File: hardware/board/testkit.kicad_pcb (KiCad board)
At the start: 2 copper layers, 100 x 100 mm, 133 parts, among them J1 Power, J12 OSC A, J13 OSC B, J14 OSC C, J15 OSC D, J3 USB_B, J4 Tag-Connect_SWD_TC2030, J5 Left, J6 Right, J7 Bottom, J8 AUDIO IN, J9 AUDIO OUT, SW1 POWER, SW2 Reset, U1 INA219BxDCN, U10 OPA4197, U11 MCP6004, U12 MCP6004, U13 MCP6004, U2 INA219BxDCN, U3 TLV76733, U4 LM4040-10, U5 ATSAMD51J20A-M, U6 AD5685R?RUZ, U7 ADG1414BRU, U8 ADG1414BRU, U9 ADG1414BRU, Y1 32.768 kHz

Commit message: Re-do the motherboard
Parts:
- removed the C20 at (94.0, 116.0)
- removed J12: OSC A, Connector_Audio:Jack_3.5mm_CUI_SJ1-3533NG_Horizontal
- removed J13: OSC B, Connector_Audio:Jack_3.5mm_CUI_SJ1-3533NG_Horizontal
- removed J14: OSC C, Connector_Audio:Jack_3.5mm_CUI_SJ1-3533NG_Horizontal
- removed J15: OSC D, Connector_Audio:Jack_3.5mm_CUI_SJ1-3533NG_Horizontal
- removed R38, R40, R42, R48, R50, R52, R54: 121k, Resistor_SMD:R_0603_1608Metric_Pad0.98x0.95mm_HandSolder
- removed R39, R41, R47, R49, R51, R53: 100k, Resistor_SMD:R_0603_1608Metric_Pad0.98x0.95mm_HandSolder
- removed R43, R44, R45, R46, R55, R56, R57, R58: 18.7k, Resistor_SMD:R_0603_1608Metric_Pad0.98x0.95mm_HandSolder
- removed R59, R60: 1k, Resistor_SMD:R_0603_1608Metric_Pad0.98x0.95mm_HandSolder
- removed REF** (x4): MountingHole_3.2mm_M3, MountingHole:MountingHole_3.2mm_M3
- removed U12, U13: MCP6004, Package_SO:TSSOP-14_4.4x5mm_P0.65mm
- added ?: , winterbloom:ermine, F.Cu at (151.4, 78.7)
- added C18: 1uF, Capacitor_SMD:C_0603_1608Metric_Pad1.08x0.95mm_HandSolder, F.Cu at (134.7, 120.9)
- added D4: 3.3, winterbloom:LED_0805_Kingbright_APT2012, F.Cu at (107.0, 54.0)
- added D5: +12V, winterbloom:LED_0805_Kingbright_APT2012, F.Cu at (104.0, 54.0)
- added D6: -12V, winterbloom:LED_0805_Kingbright_APT2012, F.Cu at (101.0, 54.0)
- added D7: ACT, winterbloom:LED_0805_Kingbright_APT2012, F.Cu at (113.0, 54.0)
- added D8: VBUS, winterbloom:LED_0805_Kingbright_APT2012, F.Cu at (110.0, 54.0)
- added G***: LOGO, winterbloom:Extra_Long_Wiggly_Boi_40mm, F.Cu at (109.8, 131.5)
- added H1: M3, MountingHole:MountingHole_3.2mm_M3_Pad_Via, F.Cu at (80.0, 54.0)
- added H2: M3, MountingHole:MountingHole_3.2mm_M3_Pad_Via, F.Cu at (80.0, 144.0)
- added H3: M3, MountingHole:MountingHole_3.2mm_M3_Pad_Via, F.Cu at (170.0, 54.0)
- added H4: M3, MountingHole:MountingHole_3.2mm_M3_Pad_Via, F.Cu at (170.0, 144.0)
- added J2: SWD, Connector_PinHeader_1.27mm:PinHeader_2x05_P1.27mm_Vertical, F.Cu at (124.2, 69.9)
- C1: value 4.7uF -> 47uF; footprint Capacitor_SMD:C_0805_2012Metric_Pad1.18x1.45mm_HandSolder -> Capacitor_THT:CP_Radial_D5.0mm_P2.50mm
- C17: value 1uF -> 0.1uF
- C2: value 0.1uF -> 47uF; footprint Capacitor_SMD:C_0603_1608Metric_Pad1.08x0.95mm_HandSolder -> Capacitor_THT:CP_Radial_D5.0mm_P2.50mm
- C25, C26, C27, C28, C29, C30, C31, C32: value 22pF -> 0.1uF
- C3: value 0.1uF -> 10uF; footprint Capacitor_SMD:C_0603_1608Metric_Pad1.08x0.95mm_HandSolder -> Capacitor_THT:CP_Radial_D5.0mm_P2.50mm
- C4: value 4.7uF -> 10uF; footprint Capacitor_SMD:C_0805_2012Metric_Pad1.18x1.45mm_HandSolder -> Capacitor_THT:CP_Radial_D5.0mm_P2.50mm
- C5: value 0.1uF -> 4.7nF
- D1, D2: value 1N5819 -> BARRIER; footprint Diode_SMD:D_SOD-123 -> winterbloom:DIODE_SOD-123_SOD-123F
- J1: value Power -> POWER; footprint Connector_PinHeader_2.54mm:PinHeader_2x05_P2.54mm_Horizontal -> Connector_Wire:SolderWire-0.75sqmm_1x03_P4.8mm_D1.25mm_OD2.3mm
- J3: value USB_B -> USB_B_Receptacle
- J4: value Tag-Connect_SWD_TC2030 -> EXT; footprint winterbloom:Tag_Connect_TC2030NL -> Connector_Wire:SolderWire-0.75sqmm_1x06_P4.8mm_D1.25mm_OD2.3mm
- J8: value AUDIO IN -> EXT; footprint Connector_Audio:Jack_3.5mm_CUI_SJ1-3533NG_Horizontal -> Connector_Wire:SolderWire-0.75sqmm_1x06_P4.8mm_D1.25mm_OD2.3mm
- J9: value AUDIO OUT -> EXT; footprint Connector_Audio:Jack_3.5mm_CUI_SJ1-3533NG_Horizontal -> Connector_Wire:SolderWire-0.75sqmm_1x06_P4.8mm_D1.25mm_OD2.3mm
- R1, R2: value 1R -> 1k; footprint Resistor_SMD:R_1210_3225Metric_Pad1.30x2.65mm_HandSolder -> Resistor_SMD:R_0603_1608Metric_Pad0.98x0.95mm_HandSolder
- R3: value 270 -> 1k
- R35, R37: value 100k -> 1k
- R36: value 121k -> 1k
- R5: value 1k -> 1M; footprint Resistor_SMD:R_0603_1608Metric_Pad0.98x0.95mm_HandSolder -> Resistor_SMD:R_0805_2012Metric_Pad1.20x1.40mm_HandSolder
- SW1: footprint Connector_PinSocket_2.54mm:PinSocket_2x02_P2.54mm_Vertical -> Connector_Wire:SolderWire-0.75sqmm_1x04_P4.8mm_D1.25mm_OD2.3mm
- U1: value INA219BxDCN -> LD1117-3.3; footprint Package_TO_SOT_SMD:SOT-23-8 -> Package_TO_SOT_SMD:SOT-223-3_TabPin2
- U2: value INA219BxDCN -> LM4040-10; footprint Package_TO_SOT_SMD:SOT-23-8 -> Package_TO_SOT_SMD:SOT-23
- U3: value TLV76733 -> LM4040-10; footprint winterbloom:TI-DGN-HVSSOP-8_3.0x3.0mm_P0.65mm -> Package_TO_SOT_SMD:SOT-23
- U4: value LM4040-10 -> MUX509; footprint Package_TO_SOT_SMD:SOT-23 -> Package_SO:TSSOP-16_4.4x5mm_P0.65mm
- U7, U8, U9: value ADG1414BRU -> MUX509; footprint Package_SO:TSSOP-24_4.4x7.8mm_P0.65mm -> Package_SO:TSSOP-16_4.4x5mm_P0.65mm
- moved R5 75.1 mm to (116.0, 54.0), turned to 90 degrees
- moved U7 73.2 mm to (89.7, 112.1), turned to 0 degrees
- moved U8 70.5 mm to (89.6, 121.1), turned to 0 degrees
- moved C30 67.2 mm to (159.3, 129.4), turned to 0 degrees
- moved U4 66.1 mm to (157.1, 133.6), turned to 0 degrees
- moved R36 64.9 mm to (151.1, 119.5)
- moved U2 64.7 mm to (148.1, 119.5), turned to 180 degrees
- moved R6 63.6 mm to (113.2, 59.0), turned to 90 degrees
- moved C32 52.0 mm to (159.7, 120.7), turned to 0 degrees
- moved C27 51.9 mm to (154.9, 129.4), turned to 180 degrees
- moved C28 50.1 mm to (154.9, 120.7), turned to 180 degrees
- moved R35 47.5 mm to (111.0, 59.0)
- moved U3 43.1 mm to (97.7, 111.5), turned to 270 degrees
- moved J3 39.4 mm to (124.7, 62.2), turned to 90 degrees
- moved C1 35.1 mm to (93.0, 62.0)
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- renumbered C18 to C20
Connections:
- net D+ renamed /MCU/D+
- net D- renamed /MCU/D-
- net DAC_1 renamed /DAC/DAC_1
- net DAC_3 renamed /DAC/DAC_3
- net Net-(U6-Pad1) renamed /DAC/DAC_VREF
- C1 pad 1: +12V -> +12VRAW
- C15 pad 1: +3V3 -> GND
- C15 pad 2: GND -> /AnalogOutBuffers/-10v_DAC
- C16 pad 1: Net-(C16-Pad1) -> +3V3
- C17 pad 1: Net-(C16-Pad1) -> /DAC/VDD_DAC
- C19 pad 1: +3V3 -> GND
- C19 pad 2: GND -> /AnalogInBuffers/-10v_ADC
- C2 pad 2: +3V3 -> -12VRAW
- C21 pad 2: A1 -> /Switching/ADC_1
- C22 pad 2: A2 -> /Switching/ADC_2
- C23 pad 2: A3 -> /Switching/ADC_3
- C24 pad 2: A4 -> /Switching/ADC_4
- C25 pad 1: Net-(C25-Pad1) -> -12V
- C25 pad 2: A5 -> GND
- C26 pad 1: Net-(C26-Pad1) -> -12V
- C26 pad 2: A6 -> GND
- C27 pad 1: Net-(C27-Pad1) -> -12V
- C27 pad 2: A7 -> GND
- C28 pad 1: Net-(C28-Pad1) -> -12V
- C28 pad 2: A8 -> GND
- C29 pad 1: Net-(C29-Pad1) -> +12V
- C29 pad 2: A9 -> GND
- C3 pad 1: GND -> +12V
- C3 pad 2: +3V3 -> GND
- C30 pad 1: Net-(C30-Pad1) -> +12V
- C30 pad 2: A10 -> GND
- C31 pad 1: Net-(C31-Pad1) -> +12V
- C31 pad 2: A11 -> GND
- C32 pad 1: Net-(C32-Pad1) -> +12V
- C32 pad 2: A12 -> GND
- C5 pad 1: GND -> Net-(C5-Pad1)
- C5 pad 2: -10V -> GND
- C6 pad 1: /MCU/VDDANA -> /MCU/ADC0.AIN1+ANAREF.VREF0
- FB3 pad 1: /MCU/VDDANA -> /MCU/ADC0.AIN1+ANAREF.VREF0
- FB4 pad 1: Net-(C16-Pad1) -> /DAC/VDD_DAC
- J1 pad 2: -12VRAW -> GND
- J1 pad 3: GND -> +12VRAW
- J3 pad 1: Net-(J3-Pad1) -> /MCU/VBUS
- J3 pad 5: GND -> Net-(C5-Pad1)
- J4 pad 1: +3V3 -> GND
- J4 pad 2: /MCU/SWDIO -> /EXT_MM_V
- J4 pad 3: /MCU/RESET -> /EXT_MM_A
- J4 pad 4: /MCU/SWCLK -> /EXT_AUDIO_A
- J4 pad 5: GND -> /EXT_AUDIO_B
- J4 pad 6: Net-(J4-Pad6) -> GND
- J5 pad 15: A1-PRE -> /IO22
- J5 pad 16: A2-PRE -> /IO23
- J5 pad 17: A3-PRE -> /IO20
- J5 pad 18: A4-PRE -> /IO21
- J5 pad 19: A5-PRE -> GND
- J5 pad 20: A6-PRE -> GND
- J5 pad 21: A7-PRE -> /ADC_1B
- J5 pad 22: A8-PRE -> /ADC_1A
- J5 pad 23: A9-PRE -> /ADC_1D
- J5 pad 24: A10-PRE -> /ADC_1C
- J5 pad 25: A11-PRE -> /ADC_4B
- J5 pad 26: A12-PRE -> /ADC_4A
- J5 pad 27: GND -> /ADC_4D
- J5 pad 28: GND -> /ADC_4C
- J5 pad 29: A13 -> GND
- J5 pad 30: A14 -> GND
- J5 pad 31: A15 -> /ADC_3B
- J5 pad 32: A16 -> /ADC_3A
- J5 pad 33: A18 -> /ADC_3D
- J5 pad 34: A17 -> /ADC_3C
- J5 pad 35: A20 -> /ADC_2B
- J5 pad 36: A19 -> /ADC_2A
- J5 pad 37: Net-(J5-Pad37) -> /ADC_2D
- J5 pad 38: Net-(J5-Pad38) -> /ADC_2C
- J5 pad 4: +12VDOWNSTREAM -> -12VDOWNSTREAM
- J5 pad 5: GND -> +12VDOWNSTREAM
- J5 pad 6: GND -> -12VDOWNSTREAM
- J5 pad 7: -12VDOWNSTREAM -> +12V
- J5 pad 8: -12VDOWNSTREAM -> -12V
- J6 pad 10: /AUDIO_IN_1A -> /EXT_MM_A
- J6 pad 11: /AUDIO_IN_1C -> /EXT_FG_A
- J6 pad 12: /AUDIO_IN_1D -> /EXT_FG_B
- J6 pad 13: GND -> /EXT_INST_A
- J6 pad 14: GND -> /EXT_INST_B
- J6 pad 15: /OSC_D -> /EXT_INST_D
- J6 pad 16: /OSC_C -> /EXT_INST_C
- J6 pad 17: /OSC_B -> GND
- J6 pad 18: /OSC_A -> GND
- J6 pad 19: GND -> /IO1
- J6 pad 20: GND -> /IO2
- J6 pad 21: /DAC_2B -> /IO3
- J6 pad 22: /DAC_2A -> /IO4
- J6 pad 23: /DAC_2C -> /IO5
- J6 pad 24: /DAC_2D -> GND
- J6 pad 25: /DAC_1B -> SERIAL1.3
- J6 pad 26: /DAC_1A -> SERIAL1.2
- J6 pad 27: /DAC_1C -> SERIAL1.1
- J6 pad 28: /DAC_1D -> SERIAL1.0
- J6 pad 3: /AUDIO_OUT_L -> /EXT_OSC_A
- J6 pad 31: /DAC_4B -> /DAC_1B
- J6 pad 32: /DAC_4A -> /DAC_1A
- J6 pad 33: /DAC_4C -> /DAC_1D
- J6 pad 34: /DAC_4D -> /DAC_1C
- J6 pad 35: /DAC_3B -> /DAC_4B
- J6 pad 36: /DAC_3A -> /DAC_4A
- J6 pad 37: /DAC_3C -> /DAC_4D
- J6 pad 38: /DAC_3D -> /DAC_4C
- J6 pad 4: /AUDIO_OUT_R -> /EXT_OSC_B
- J6 pad 5: /AUDIO_IN_2B -> /EXT_OSC_D
- J6 pad 6: /AUDIO_IN_2A -> /EXT_OSC_C
- J6 pad 7: /AUDIO_IN_2C -> /EXT_AUDIO_A
- J6 pad 8: /AUDIO_IN_2D -> /EXT_AUDIO_B
- J6 pad 9: /AUDIO_IN_1B -> /EXT_MM_V
- J7 pad 10: GND -> /IO14
- J7 pad 11: SERIAL4.0 -> GND
- J7 pad 13: SERIAL4.1 -> /IO11
- J7 pad 14: GND -> /IO12
- J7 pad 15: SERIAL4.2 -> /IO9
- J7 pad 16: GND -> /IO10
- J7 pad 17: SERIAL4.3 -> GND
- J7 pad 19: DB0 -> GND
- J7 pad 21: GND -> /IO7
- J7 pad 22: GND -> /IO8
- J7 pad 23: SERIAL1.0 -> SERIAL4.1
- J7 pad 24: GND -> SERIAL4.0
- J7 pad 25: SERIAL1.1 -> SERIAL4.3
- J7 pad 26: GND -> SERIAL4.2
- J7 pad 27: SERIAL1.2 -> /IO6
- J7 pad 29: SERIAL1.3 -> GND
- J7 pad 3: GND -> /IO19
- J7 pad 31: DR4 -> /DAC_3D
- J7 pad 32: GND -> /DAC_3C
- J7 pad 33: DR3 -> /DAC_3B
- J7 pad 34: GND -> /DAC_3A
- J7 pad 35: DR2 -> /DAC_2D
- J7 pad 36: GND -> /DAC_2C
- J7 pad 37: DR1 -> /DAC_2B
- J7 pad 38: GND -> /DAC_2A
- J7 pad 4: GND -> Net-(J7-Pad4)
- J7 pad 5: GND -> /IO17
- J7 pad 6: GND -> /IO18
- J7 pad 7: DB1 -> /IO15
- J7 pad 8: GND -> /IO16
- J7 pad 9: DB2 -> /IO13
- R1 pad 1: +12VRAW -> +3V3
- R1 pad 2: +12VMONITORED -> Net-(D4-Pad2)
- R10 pad 2: -10V -> /AnalogOutBuffers/-10v_DAC
- R12 pad 2: -10V -> /AnalogOutBuffers/-10v_DAC
- R13 pad 2: DAC_4 -> /DAC/DAC_4
- R14 pad 2: -10V -> /AnalogOutBuffers/-10v_DAC
- R15 pad 1: /Switching/DAC_3 -> /Switching/DAC_1
- R16 pad 1: /Switching/DAC_4 -> /Switching/DAC_2
- R17 pad 1: /Switching/DAC_1 -> /Switching/DAC_3
- R18 pad 1: /Switching/DAC_2 -> /Switching/DAC_4
- R19 pad 1: /Switching/DAC_3 -> /Switching/DAC_1
- R2 pad 1: -12VMONITORED -> +12V
- R2 pad 2: -12VRAW -> Net-(D5-Pad2)
- R20 pad 1: /Switching/DAC_4 -> /Switching/DAC_2
- R21 pad 1: /Switching/DAC_1 -> /Switching/DAC_3
- R22 pad 1: /Switching/DAC_2 -> /Switching/DAC_4
- R23 pad 2: A1-PRE -> /MCU/A1
- R24 pad 2: -10V -> /AnalogInBuffers/-10v_ADC
- R25 pad 2: A2-PRE -> /MCU/A2
- R26 pad 2: -10V -> /AnalogInBuffers/-10v_ADC
- R27 pad 2: A3-PRE -> /MCU/A3
- R28 pad 2: -10V -> /AnalogInBuffers/-10v_ADC
- R29 pad 2: A4-PRE -> /MCU/A4
- R3 pad 1: -12V -> GND
- R3 pad 2: -10V -> Net-(D6-Pad2)
- R30 pad 2: -10V -> /AnalogInBuffers/-10v_ADC
- R31 pad 1: A1 -> /Switching/ADC_1
- R32 pad 1: A2 -> /Switching/ADC_2
- R33 pad 1: A3 -> /Switching/ADC_3
- R34 pad 1: A4 -> /Switching/ADC_4
- R35 pad 1: Net-(C25-Pad1) -> /MCU/VBUS
- R35 pad 2: A5-PRE -> Net-(D8-Pad2)
- R36 pad 1: Net-(C25-Pad1) -> -12V
- R36 pad 2: -10V -> /AnalogOutBuffers/-10v_DAC
- R37 pad 1: Net-(C26-Pad1) -> -12V
- R37 pad 2: A6-PRE -> /AnalogInBuffers/-10v_ADC
- R5 pad 1: +3V3 -> Net-(C5-Pad1)
- R5 pad 2: Net-(R5-Pad2) -> GND
- R6 pad 1: +3V3 -> /IO23
- R6 pad 2: Net-(R6-Pad2) -> Net-(D7-Pad2)
- R8 pad 2: -10V -> /AnalogOutBuffers/-10v_DAC
- R9 pad 2: DAC_2 -> /DAC/DAC_2
- SW1 pad 1: -12VMONITORED -> -12V
- SW1 pad 3: +12VMONITORED -> +12V
- U1 pad 1: +12VRAW -> GND
- U1 pad 2: +12VMONITORED -> +3V3
- U1 pad 3: GND -> +12V
- U11 pad 1: A1 -> /Switching/ADC_1
- U11 pad 14: A4 -> /Switching/ADC_4
- U11 pad 7: A2 -> /Switching/ADC_2
- U11 pad 8: A3 -> /Switching/ADC_3
- U2 pad 1: -12VMONITORED -> GND
- U2 pad 2: -12VRAW -> /AnalogOutBuffers/-10v_DAC
- U2 pad 3: GND -> (no net)
- U3 pad 1: +3V3 -> GND
- U3 pad 2: +3V3 -> /AnalogInBuffers/-10v_ADC
- U3 pad 3: Net-(U3-Pad3) -> (no net)
- U4 pad 1: GND -> /Switching/DAC_A0
- U4 pad 2: -10V -> +12V
- U4 pad 3: (no net) -> -12V
- U5 pad 10: A10 -> /IO17
- U5 pad 11: A11 -> /MCU/A3
- U5 pad 12: A12 -> /MCU/A2
- U5 pad 13: A13 -> /IO16
- U5 pad 14: A14 -> /IO15
- U5 pad 15: A15 -> /IO14
- U5 pad 16: A16 -> /IO13
- U5 pad 17: A18 -> /IO12
- U5 pad 18: A17 -> /IO11
- U5 pad 19: A20 -> /IO10
- U5 pad 20: A19 -> /IO9
- U5 pad 23: DB1 -> /IO8
- U5 pad 24: DB2 -> /IO7
- U5 pad 29: DB0 -> /IO6
- U5 pad 3: A5 -> /IO19
- U5 pad 30: SPI_SCLK -> /DAC/SPI_COPI
- U5 pad 32: SPI_COPI -> /MCU/SPI_COPI
- U5 pad 39: DR4 -> /Switching/DAC_A0
- U5 pad 4: A6 -> /MCU/ADC0.AIN1+ANAREF.VREF0
- U5 pad 40: DR3 -> /Switching/DAC_A1
- U5 pad 41: DR2 -> /IO5
- U5 pad 42: DR1 -> /IO4
- U5 pad 49: /MCU/PB22 -> /IO3
- U5 pad 5: A7 -> /MCU/A1
- U5 pad 50: /MCU/PB23 -> /IO2
- U5 pad 51: /MCU/PA27 -> /IO1
- U5 pad 59: I2C_SDA -> /IO23
- U5 pad 6: A8 -> /MCU/A4
- U5 pad 60: I2C_SCL -> /IO22
- U5 pad 61: A1 -> /IO21
- U5 pad 62: A2 -> /IO20
- U5 pad 63: A3 -> /Switching/ADC_A0
- U5 pad 64: A4 -> /Switching/ADC_A1
- U5 pad 8: /MCU/VDDANA -> /MCU/ADC0.AIN1+ANAREF.VREF0
- U5 pad 9: A9 -> /IO18
- U6 pad 12: SPI_SCLK -> /MCU/SPI_COPI
- U6 pad 14: SPI_COPI -> /DAC/SPI_COPI
- U6 pad 2: DAC_2 -> /DAC/DAC_4
- U6 pad 5: Net-(C16-Pad1) -> /DAC/VDD_DAC
- U6 pad 7: DAC_4 -> /DAC/DAC_2
- U7 pad 1: SPI_SCLK -> /Switching/ADC_A0
- U7 pad 10: /AUDIO_IN_1C -> /ADC_4D
- U7 pad 11: /AUDIO_IN_L -> /ADC_4C
- U7 pad 12: /AUDIO_IN_1D -> /ADC_4B
- U7 pad 13: /AUDIO_IN_2A -> /ADC_4A
- U7 pad 14: /AUDIO_IN_R -> +12V
- U7 pad 15: /AUDIO_IN_2B -> GND
- U7 pad 16: /AUDIO_IN_R -> /Switching/ADC_A1
- U7 pad 3: SPI_COPI -> -12V
- U7 pad 4: GND -> /ADC_1A
- U7 pad 5: /AUDIO_IN_L -> /ADC_1B
- U7 pad 6: /AUDIO_IN_1A -> /ADC_1C
- U7 pad 7: /AUDIO_IN_L -> /ADC_1D
- U7 pad 8: /AUDIO_IN_1B -> /Switching/ADC_1
- U7 pad 9: /AUDIO_IN_L -> /Switching/ADC_4
- U8 pad 1: SPI_SCLK -> /Switching/ADC_A0
- U8 pad 10: /DAC_1C -> /ADC_2D
- U8 pad 11: /Switching/DAC_1 -> /ADC_2C
- U8 pad 12: /DAC_1D -> /ADC_2B
- U8 pad 13: /DAC_2A -> /ADC_2A
- U8 pad 14: /Switching/DAC_2 -> +12V
- U8 pad 15: /DAC_2B -> GND
- U8 pad 16: /Switching/DAC_2 -> /Switching/ADC_A1
- U8 pad 3: Net-(R5-Pad2) -> -12V
- U8 pad 4: GND -> /ADC_3A
- U8 pad 5: /Switching/DAC_1 -> /ADC_3B
- U8 pad 6: /DAC_1A -> /ADC_3C
- U8 pad 7: /Switching/DAC_1 -> /ADC_3D
- U8 pad 8: /DAC_1B -> /Switching/ADC_3
- U8 pad 9: /Switching/DAC_1 -> /Switching/ADC_2
- U9 pad 1: SPI_SCLK -> /Switching/DAC_A0
- U9 pad 10: /DAC_3C -> /DAC_4D
- U9 pad 11: /Switching/DAC_3 -> /DAC_4C
- U9 pad 12: /DAC_3D -> /DAC_4B
- U9 pad 14: /Switching/DAC_4 -> +12V
- U9 pad 15: /DAC_4B -> GND
- U9 pad 16: /Switching/DAC_4 -> /Switching/DAC_A1
- U9 pad 3: Net-(R6-Pad2) -> -12V
- U9 pad 4: GND -> /DAC_1A
- U9 pad 5: /Switching/DAC_3 -> /DAC_1B
- U9 pad 6: /DAC_3A -> /DAC_1C
- U9 pad 7: /Switching/DAC_3 -> /DAC_1D
- U9 pad 8: /DAC_3B -> /Switching/DAC_1
- U9 pad 9: /Switching/DAC_3 -> /Switching/DAC_4
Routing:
- net -10V: track 208.9 -> 0.00 mm, vias 9 -> 0
- net +12V: track 129.0 -> 250.2 mm, vias 6 -> 7
- net +3V3: track 348.1 -> 237.4 mm, vias 14 -> 34
- net SPI_SCLK: track 90.9 -> 0.00 mm, vias 4 -> 0
- net -12V: track 139.0 -> 229.5 mm, vias 6 -> 5
- net /IO23: track 0.00 -> 88.4 mm
- net /OSC_A: track 86.7 -> 0.00 mm
- net /Switching/ADC_A0: track 0.00 -> 80.3 mm, vias 0 -> 3
- net /IO19: track 0.00 -> 79.2 mm, vias 0 -> 2
- net /OSC_B: track 79.1 -> 0.00 mm
- net /Switching/DAC_A0: track 0.00 -> 78.3 mm, vias 0 -> 5
- net /IO18: track 0.00 -> 72.6 mm, vias 0 -> 2
- net /Switching/ADC_A1: track 0.00 -> 71.5 mm, vias 0 -> 2
- net /IO21: track 0.00 -> 71.1 mm
- net /IO22: track 0.00 -> 69.1 mm
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- added copper zone on B.Cu, net +3V3
- added copper zone on F.Cu, net +3V3
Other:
- board text added: "+12"
- board text added: "+12V"
- board text added: "+12V SW"
- board text added: "-"
- board text added: "-12"
- board text added: "1"
- board text added: "1.1"
- board text added: "1.3"
- board text added: "10"
- board text added: "12"
- board text added: "14"
- board text added: "16"
- board text added: "18"
- board text added: "1A"
- board text added: "1B"
- board text added: "1C"
- board text added: "1D"
- board text added: "21"
- board text added: "23"
- board text added: "2A"
- board text added: "2C"
- board text added: "3"
- board text added: "3A"
- board text added: "3C"
- board text added: "3D"
- board text added: "3V3"
- board text added: "4.0"
- board text added: "4.2"
- board text added: "4A"
- board text added: "4B"
- board text added: "4C"
- board text added: "4D"
- board text added: "5"
- board text added: "8"
- board text added: "A"
- board text added: "A1B"
- board text added: "A1D"
- board text added: "A2B"
- board text added: "A2D"
- board text added: "A3B"
- board text added: "A4B"
- board text added: "A4C"
- board text added: "AUD B"
- board text added: "AUDA"
- board text added: "AUDB"
- board text added: "D"
- board text added: "D1A"
- board text added: "D1C"
- board text added: "D2B"
- board text added: "D2D"
- board text added: "D3B"
- board text added: "D3D"
- board text added: "D4A"
- board text added: "D4C"
- board text added: "FG B"
- board text added: "FGA"
- board text added: "FGB"
- board text added: "GND"
- board text added: "INST B"
- board text added: "INST C"
- board text added: "INSTA"
- board text added: "INSTB"
- board text added: "INSTC"
- board text added: "INSTD"
- board text added: "IO"
- board text added: "IO11"
- board text added: "IO13"
- board text added: "IO15"
- board text added: "IO17"
- board text added: "IO19"
- board text added: "IO2"
- board text added: "IO20"
- board text added: "IO22"
- board text added: "IO4"
- board text added: "IO6"
- board text added: "IO7"
- board text added: "IO9"
- board text added: "MM A"
- board text added: "MMA"
- board text added: "MMV"
- board text added: "OSC B"
- board text added: "OSC C"
- board text added: "OSCA"
- board text added: "OSCB"
- board text added: "OSCC"
- board text added: "OSCD"
- board text added: "SER1.0"
- board text added: "SER1.2"
- board text added: "SER4.1"
- board text added: "SER4.3"
- board text added: "TestKit Motherboard v1 10/22/2021 CERN-OHL-P V2"
- board text added: "USB"
- board text added: "V"

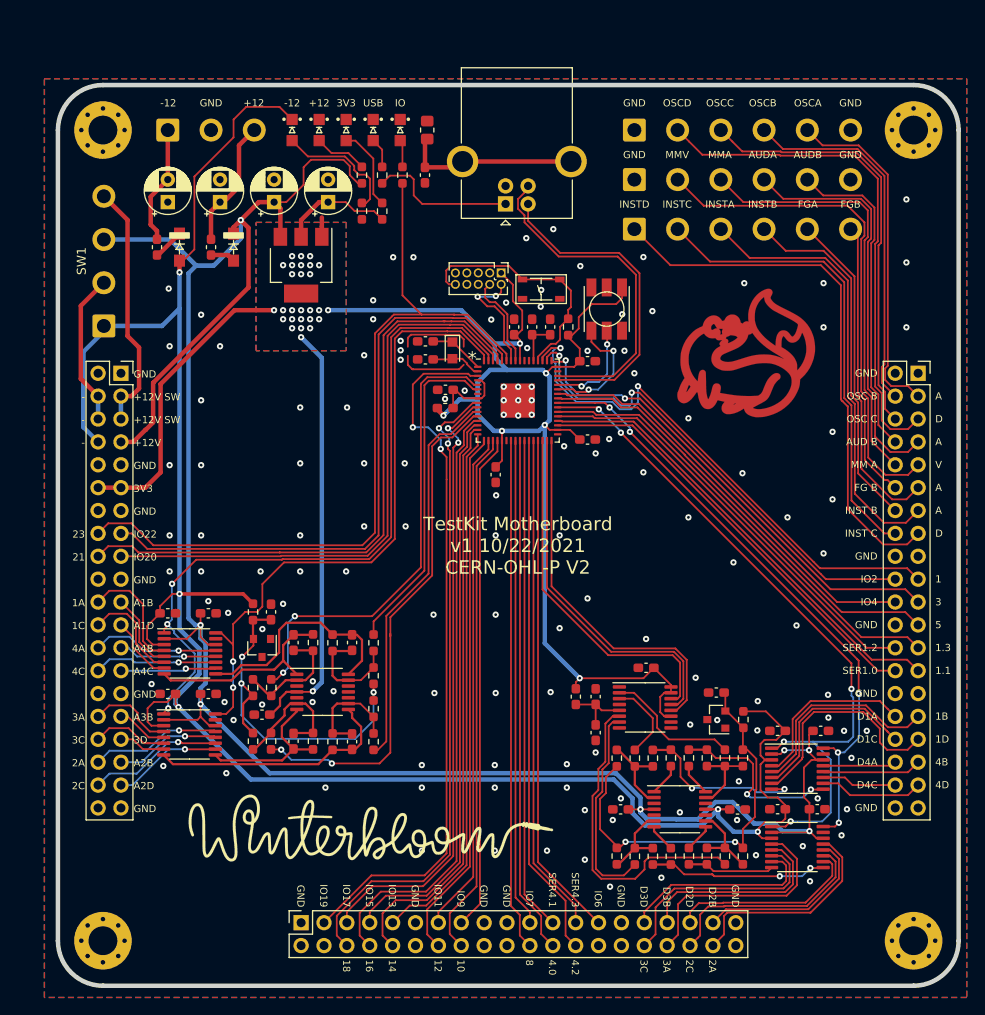
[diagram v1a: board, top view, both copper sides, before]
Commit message: Fix issues found in hardware v1
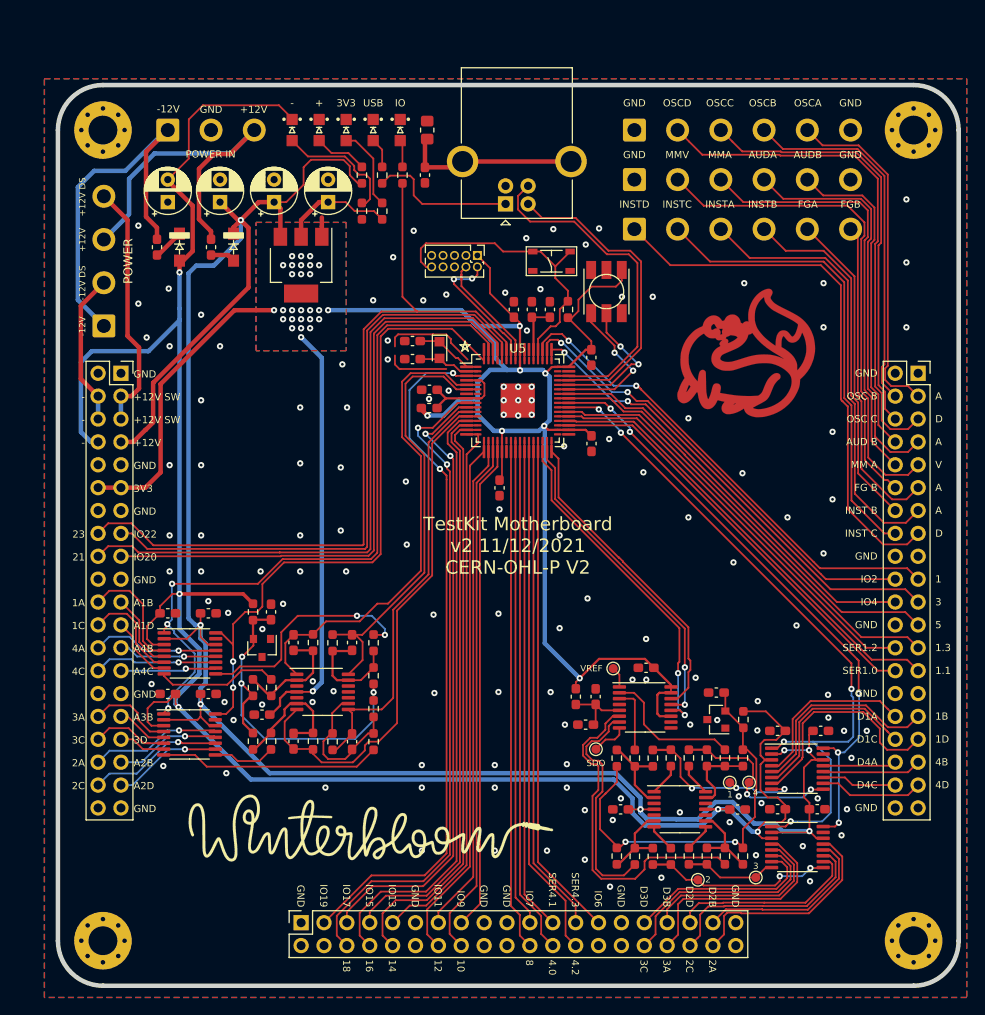
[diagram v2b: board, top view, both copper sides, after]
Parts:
- added TP1: SDO, TestPoint:TestPoint_Pad_D1.0mm, F.Cu at (134.7, 122.7)
- added TP2: VREF, TestPoint:TestPoint_Pad_D1.0mm, F.Cu at (136.7, 113.8)
- added TP3: 1, TestPoint:TestPoint_Pad_D1.0mm, F.Cu at (149.6, 126.4)
- added TP4: 2, TestPoint:TestPoint_Pad_D1.0mm, F.Cu at (146.1, 137.2)
- added TP5: 3, TestPoint:TestPoint_Pad_D1.0mm, F.Cu at (152.5, 137.0)
- added TP6: 4, TestPoint:TestPoint_Pad_D1.0mm, F.Cu at (151.7, 126.4)
- R1, R2, R3, R35, R6: value 1k -> 10k
- R36: value 1k -> 270
- U5: footprint Package_DFN_QFN:QFN-64-1EP_9x9mm_P0.5mm_EP3.8x3.8mm -> winterbloom:QFN+QFP-64-SAMD51
- moved SW2 3.30 mm to (129.8, 68.6)
- moved J2 3.28 mm to (121.6, 67.9)
- moved C10 1.94 mm to (127.6, 73.9)
- moved C13 1.94 mm to (125.6, 73.9)
- moved C9 1.94 mm to (129.6, 73.9)
- moved D3 1.94 mm to (135.9, 71.9)
- moved R4 1.94 mm to (131.6, 73.9)
- moved C6 1.78 mm to (116.2, 82.8)
- moved FB3 1.78 mm to (116.2, 84.9)
- moved C11 1.53 mm to (124.0, 93.7)
- moved C7 1.43 mm to (114.4, 77.4)
- moved C8 1.43 mm to (114.4, 79.4)
- moved Y1 1.43 mm to (117.4, 78.4)
- moved C18 1.42 mm to (133.6, 120.0), turned to 180 degrees
- moved C14 0.63 mm to (134.2, 88.8), turned to 270 degrees
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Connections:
- C1 pad 1: +12VRAW -> +12V
- C2 pad 2: -12VRAW -> -12V
- C21 pad 2: /Switching/ADC_1 -> /MCU/A1
- C22 pad 2: /Switching/ADC_2 -> /MCU/A2
- C23 pad 2: /Switching/ADC_3 -> /MCU/A3
- C24 pad 2: /Switching/ADC_4 -> /MCU/A4
- R23 pad 2: /MCU/A1 -> /Switching/ADC_1
- R25 pad 2: /MCU/A2 -> /Switching/ADC_2
- R27 pad 2: /MCU/A3 -> /Switching/ADC_3
- R29 pad 2: /MCU/A4 -> /Switching/ADC_4
- R31 pad 1: /Switching/ADC_1 -> /MCU/A1
- R32 pad 1: /Switching/ADC_2 -> /MCU/A2
- R33 pad 1: /Switching/ADC_3 -> /MCU/A3
- R34 pad 1: /Switching/ADC_4 -> /MCU/A4
- SW1 pad 1: -12V -> -12VRAW
- SW1 pad 3: +12V -> +12VRAW
- U11 pad 1: /Switching/ADC_1 -> /MCU/A1
- U11 pad 14: /Switching/ADC_4 -> /MCU/A4
- U11 pad 7: /Switching/ADC_2 -> /MCU/A2
- U11 pad 8: /Switching/ADC_3 -> /MCU/A3
- U5 pad 30: /DAC/SPI_COPI -> /MCU/SPI_SCK
- U5 pad 32: /MCU/SPI_COPI -> /DAC/SPI_COPI
- U6 pad 1: /DAC/DAC_VREF -> Net-(TP2-Pad1)
- U6 pad 12: /MCU/SPI_COPI -> /MCU/SPI_SCK
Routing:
- net /MCU/SPI_COPI: track 41.3 -> 0.00 mm
- net /MCU/SPI_SCK: track 0.00 -> 38.9 mm, vias 0 -> 2
- net -12VRAW: track 13.2 -> 42.9 mm
- net +12VRAW: track 14.3 -> 40.3 mm
- net +3V3: track 237.4 -> 253.5 mm, vias 34 -> 35
- net /MCU/A4: track 36.5 -> 49.6 mm
- net /Switching/ADC_2: track 17.3 -> 7.00 mm
- net /Switching/ADC_1: track 22.1 -> 13.6 mm
- net +12V: track 250.2 -> 241.8 mm
- net /MCU/RESET: track 27.2 -> 34.6 mm
- net /MCU/DOTSTAR_CI: track 11.0 -> 17.1 mm
- net /MCU/A3: track 43.6 -> 48.2 mm
- net -12V: track 229.5 -> 233.8 mm
- net Net-(C23-Pad1): track 12.2 -> 16.3 mm
- net Net-(TP1-Pad1): track 0.00 -> 4.04 mm
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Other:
- board text added: "+"
- board text added: "+12V DS"
- board text added: "-12V"
- board text added: "-12V DS"
- board text added: "POWER IN"
- board text added: "TestKit Motherboard v2 11/12/2021 CERN-OHL-P V2"
- board text removed: "*"
- board text removed: "+12"
- board text removed: "-12"
- board text removed: "TestKit Motherboard v1 10/22/2021 CERN-OHL-P V2"
